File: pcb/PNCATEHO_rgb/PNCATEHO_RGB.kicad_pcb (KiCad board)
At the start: 2 copper layers, 93.5 x 54.1 mm, 22 parts, among them SW1 SW_PUSH, SW10 SW_PUSH, SW2 SW_PUSH, SW3 SW_PUSH, SW4 SW_PUSH, SW5 SW_PUSH, SW6 SW_PUSH, SW7 SW_PUSH, SW8 SW_PUSH, SW9 SW_PUSH, U1 ProMicro_r

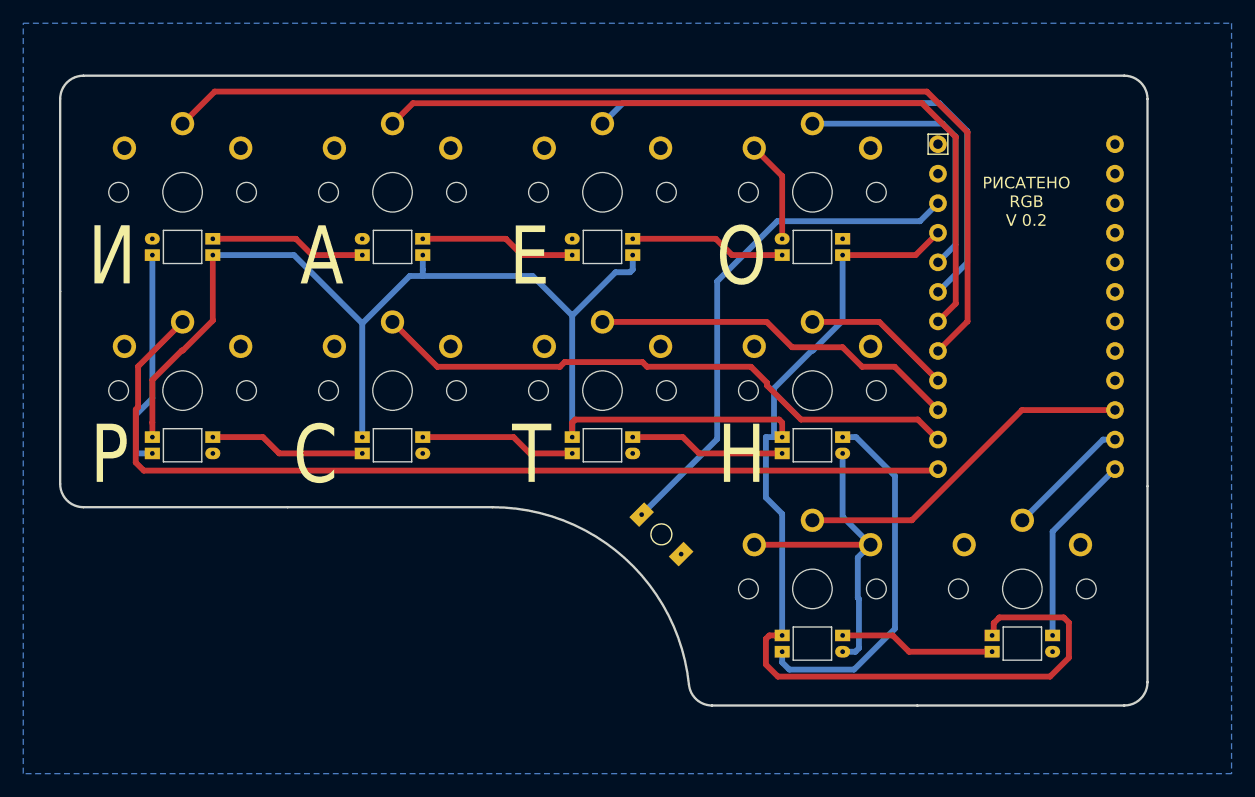
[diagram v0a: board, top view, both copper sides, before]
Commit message: update pcb files to KiCAD 7.0
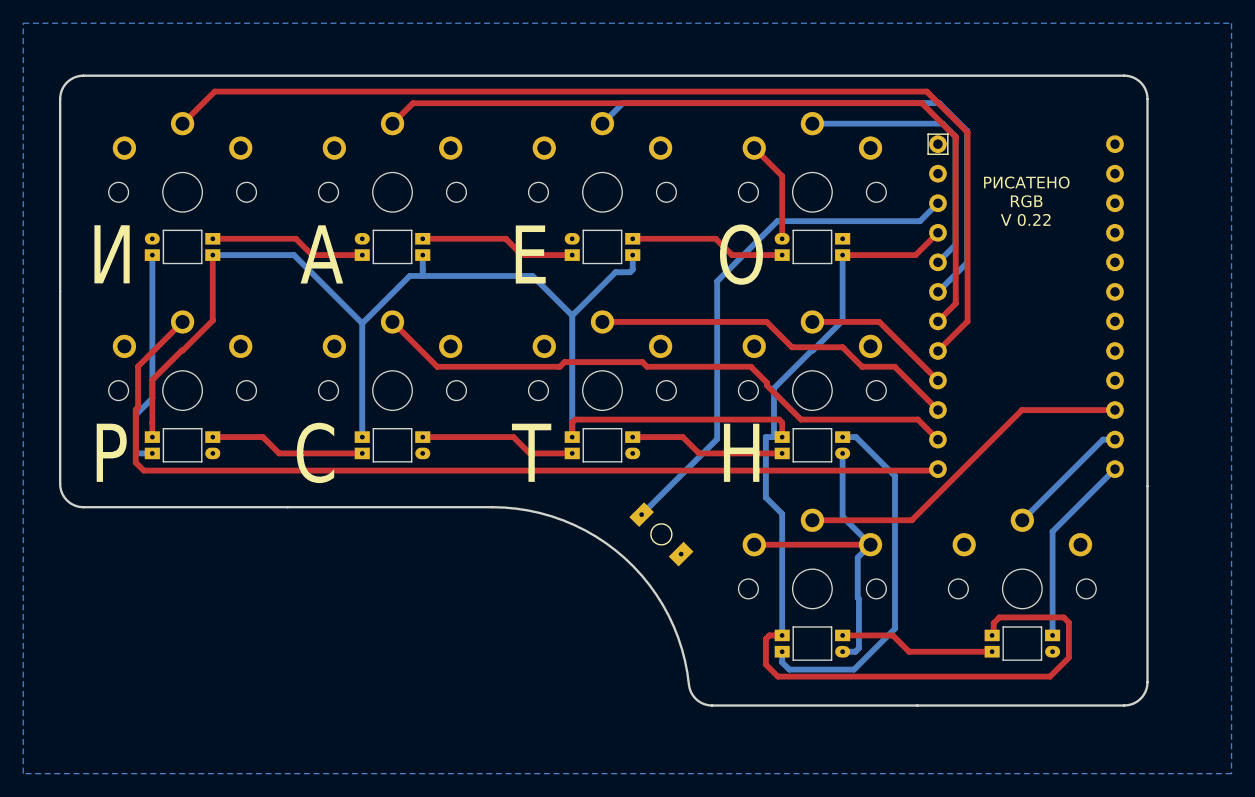
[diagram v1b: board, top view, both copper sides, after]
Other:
- net class Default removed
- board text added: "РИСАТЕНО RGB V 0.22"
- board text removed: "РИСАТЕНО RGB V 0.2"
